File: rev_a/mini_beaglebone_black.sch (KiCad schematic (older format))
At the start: 4 parts

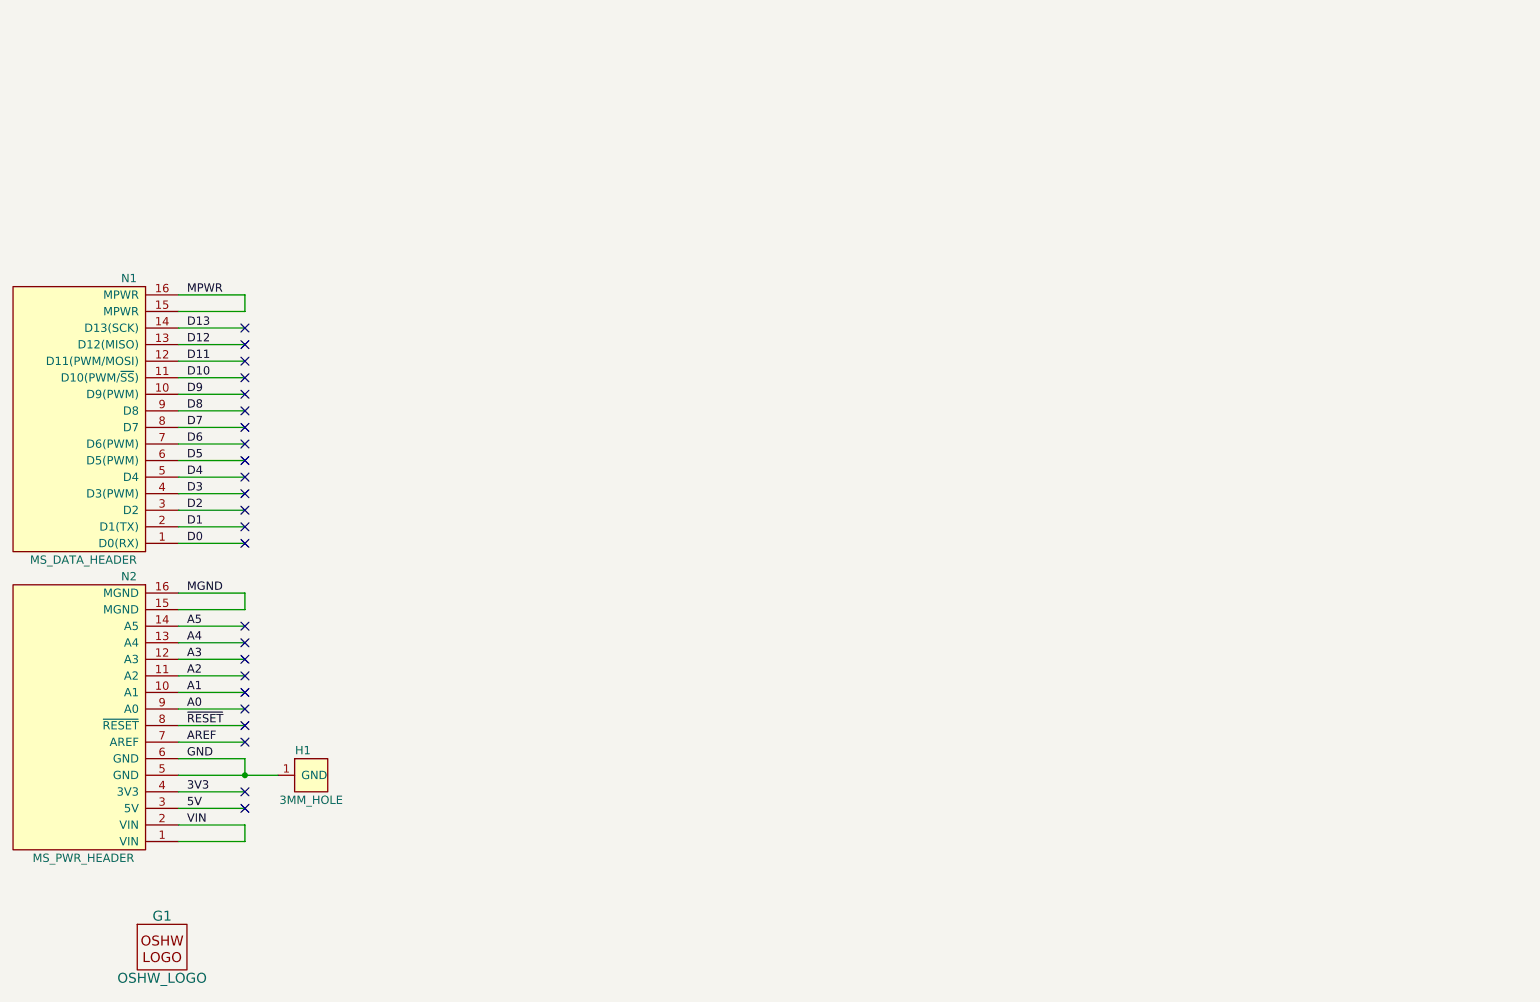
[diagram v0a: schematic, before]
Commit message: Got first layout of BBB Mini-Shield done.
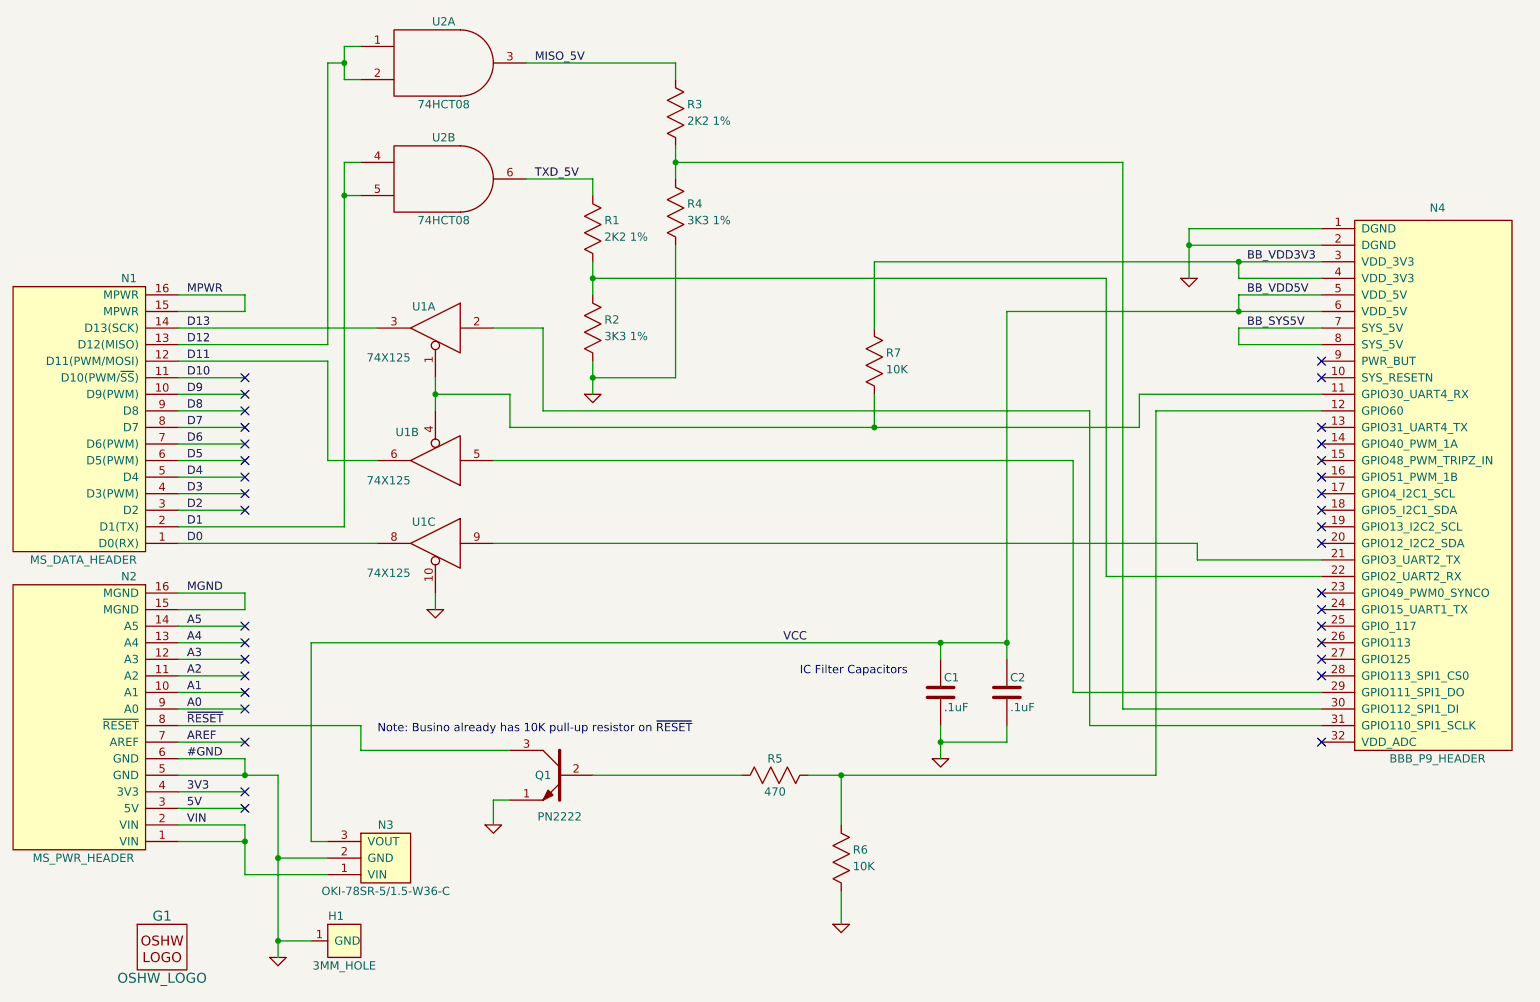
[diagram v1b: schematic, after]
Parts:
- added C1, C2: .1uF, symbol C_VERT
- added N3: OKI-78SR-5/1.5-W36-C, symbol REGULATOR_CONNECTOR
- added N4: BBB_P9_HEADER, symbol BBB_P9_HEADER
- added Q1: PN2222, symbol NPN
- added R1, R3: 2K2 1%, symbol R_VERT
- added R2, R4: 3K3 1%, symbol R_VERT
- added R5: 470, symbol R_HORIZ
- added R6, R7: 10K, symbol R_VERT
- added U1: 74X125, symbol 74X125
- added U2: 74HCT08, symbol 74X08
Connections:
- net D0: now also U1.8
- net D1: now also U2.4, U2.5
- net D11: now also U1.6
- net D12: now also U2.1, U2.2
- net D13: now also U1.3
- net GND: now also C1.2, C2.2, N3.2 (GND), N4.1 (DGND), N4.2 (DGND), Q1.1, R2.1, R4.1, R6.1, U1.10, U1.7 (GND), U1.7 (GND), U1.7 (GND), U2.7 (GND), U2.7 (GND)
- net VIN: now also N3.1 (VIN)
- net ~RESET: now also Q1.3
- new net: Q1.2, R5.1
- new net: N4.12 (GPIO60), R5.2, R6.2
- new net: N4.22 (GPIO2_UART2_RX), R1.1, R2.2
- new net: N4.30 (GPIO112_SPI1_DI), R3.1, R4.2
- new net: N4.11 (GPIO30_UART4_RX), R7.1, U1.1, U1.4
- new net: N4.31 (GPIO110_SPI1_SCLK), U1.2
- new net: N4.29 (GPIO111_SPI1_DO), U1.5
- new net: N4.21 (GPIO3_UART2_TX), U1.9
- new net BB_SYS5V: N4.7 (SYS_5V), N4.8 (SYS_5V)
- new net BB_VDD3V3: N4.3 (VDD_3V3), N4.4 (VDD_3V3), R7.2
- new net MISO_5V: R3.2, U2.3
- new net TXD_5V: R1.2, U2.6
- new net VCC: C1.1, C2.1, N3.3 (VOUT), N4.5 (VDD_5V), N4.6 (VDD_5V), U1.14 (VCC), U1.14 (VCC), U1.14 (VCC), U2.14 (VCC), U2.14 (VCC)
- no-connect marks 24 -> 35
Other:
- note added: "IC Filter Capacitors"
- note added: "Note: Busino already has 10K pull-up resistor on ~RESET"
- moved on the sheet: H1
